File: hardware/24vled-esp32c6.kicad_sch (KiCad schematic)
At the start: 5 parts, among them J1 Conn_01x20, J2 Conn_01x20, J3 Barrel_Jack, J5 2604-1106, U1 LM2596S-5

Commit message: hardware v1
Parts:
- removed J1, J2: Conn_01x20, Connector_PinHeader_2.54mm:PinHeader_1x20_P2.54mm_Vertical, symbol Connector_Generic:Conn_01x20
- removed U1: LM2596S-5, Package_TO_SOT_SMD:TO-263-5_TabPin3, symbol Regulator_Switching:LM2596S-5
- added Q1, Q2, Q3, Q4, Q5: AO3400A, Package_TO_SOT_SMD:SOT-23, symbol Transistor_FET:AO3400A
- added R1, R3, R5, R7, R9: 100, Resistor_SMD:R_0201_0603Metric, symbol Device:R
- added R10, R2, R4, R6, R8: 10k, Resistor_SMD:R_0201_0603Metric, symbol Device:R
- added U1: R-78E5.0-1.0, Converter_DCDC:Converter_DCDC_RECOM_R-78E-0.5_THT, symbol Regulator_Switching:R-78E5.0-1.0
- added U2: ~, Library:Waveshare ESP32c6, symbol Symbols:Waveshare_ESP32c6
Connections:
- net +5V: now also U1.3 (OUT), U2.14 (Pin_14)
- net GND: now also J3.2, Q1.3 (D), Q2.3 (D), Q3.3 (D), Q4.3 (D), Q5.3 (D), R10.2, R2.2, R4.2, R6.2, R8.2, U1.2 (GND), U2.15 (Pin_15)
- net +24V: now reaches J5.1 (1_1)
- net +24V: now also J3.1, U1.1 (IN)
- net WW24: now reaches J5.11 (6_1)
- net WW24: now also Q5.2 (S)
- net R24: now reaches J5.3 (2_1)
- net R24: now also Q1.2 (S)
- net G24: now reaches J5.5 (3_1)
- net G24: now also Q2.2 (S)
- net B24: now reaches J5.7 (4_1)
- net B24: now also Q3.2 (S)
- net CW24: now reaches J5.9 (5_1)
- net CW24: now also Q4.2 (S)
- new net: Q2.1 (G), R3.2, R4.1
- new net: Q3.1 (G), R5.2, R6.1
- new net: Q5.1 (G), R10.1, R9.2
- new net: Q1.1 (G), R1.2, R2.1
- new net: Q4.1 (G), R7.2, R8.1
- new net B3.3: R5.1, U2.10 (Pin_10)
- new net CW3.3: R7.1, U2.12 (Pin_12)
- new net G3.3: R3.1, U2.8 (Pin_8)
- new net R3.3: R1.1, U2.7 (Pin_7)
- new net WW3.3: R9.1, U2.13 (Pin_13)
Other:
- moved on the sheet: J3, J5

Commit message: hardware v2
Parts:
- removed J5: 2604-1106, Wago:CONN6_2604-1106_WAG, symbol Wago:2604-1106
- added J1: 2601-1106, External:26011106, symbol External:2601-1106
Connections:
- net +24V: now also J1.1 (1.1)
- net B24: now also J1.7 (4.1)
- net CW24: now also J1.9 (5.1)
- net CW3.3: now also U2.8 (Pin_8); no longer U2.12 (Pin_12)
- net G24: now also J1.5 (3.1)
- net G3.3: now also U2.12 (Pin_12); no longer U2.8 (Pin_8)
- net R24: now also J1.3 (2.1)
- net R3.3: now also U2.13 (Pin_13); no longer U2.7 (Pin_7)
- net WW24: now also J1.11 (6.1)
- net WW3.3: now also U2.7 (Pin_7); no longer U2.13 (Pin_13)

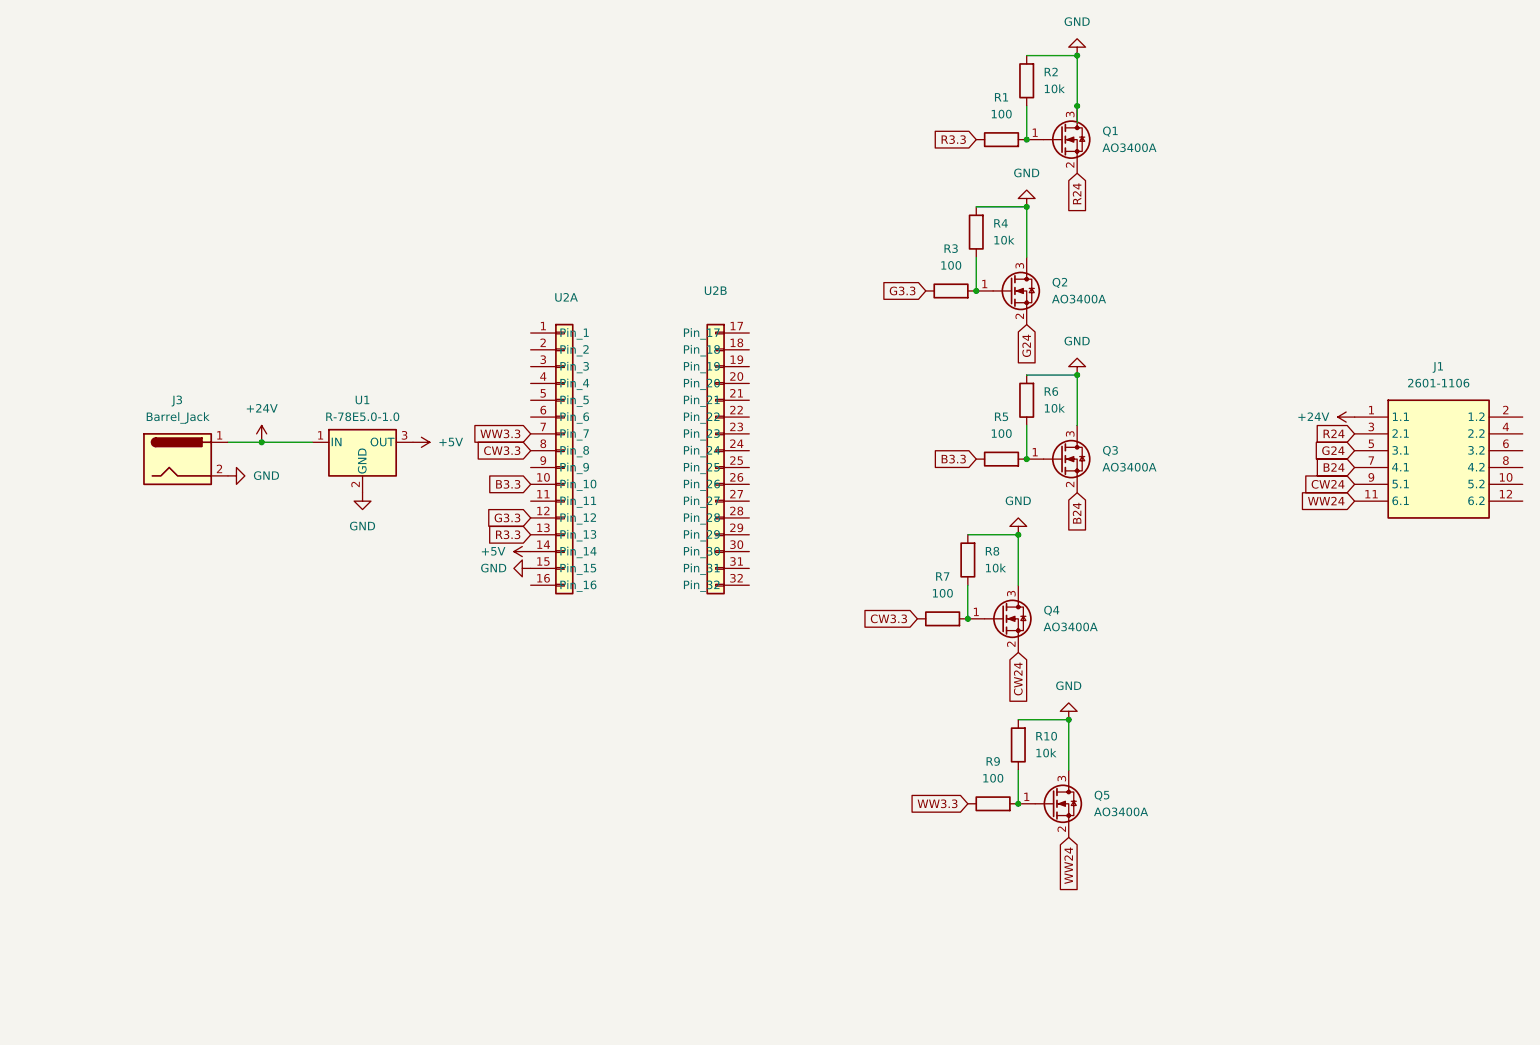
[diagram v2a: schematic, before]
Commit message: fix schematic warnings and kibot
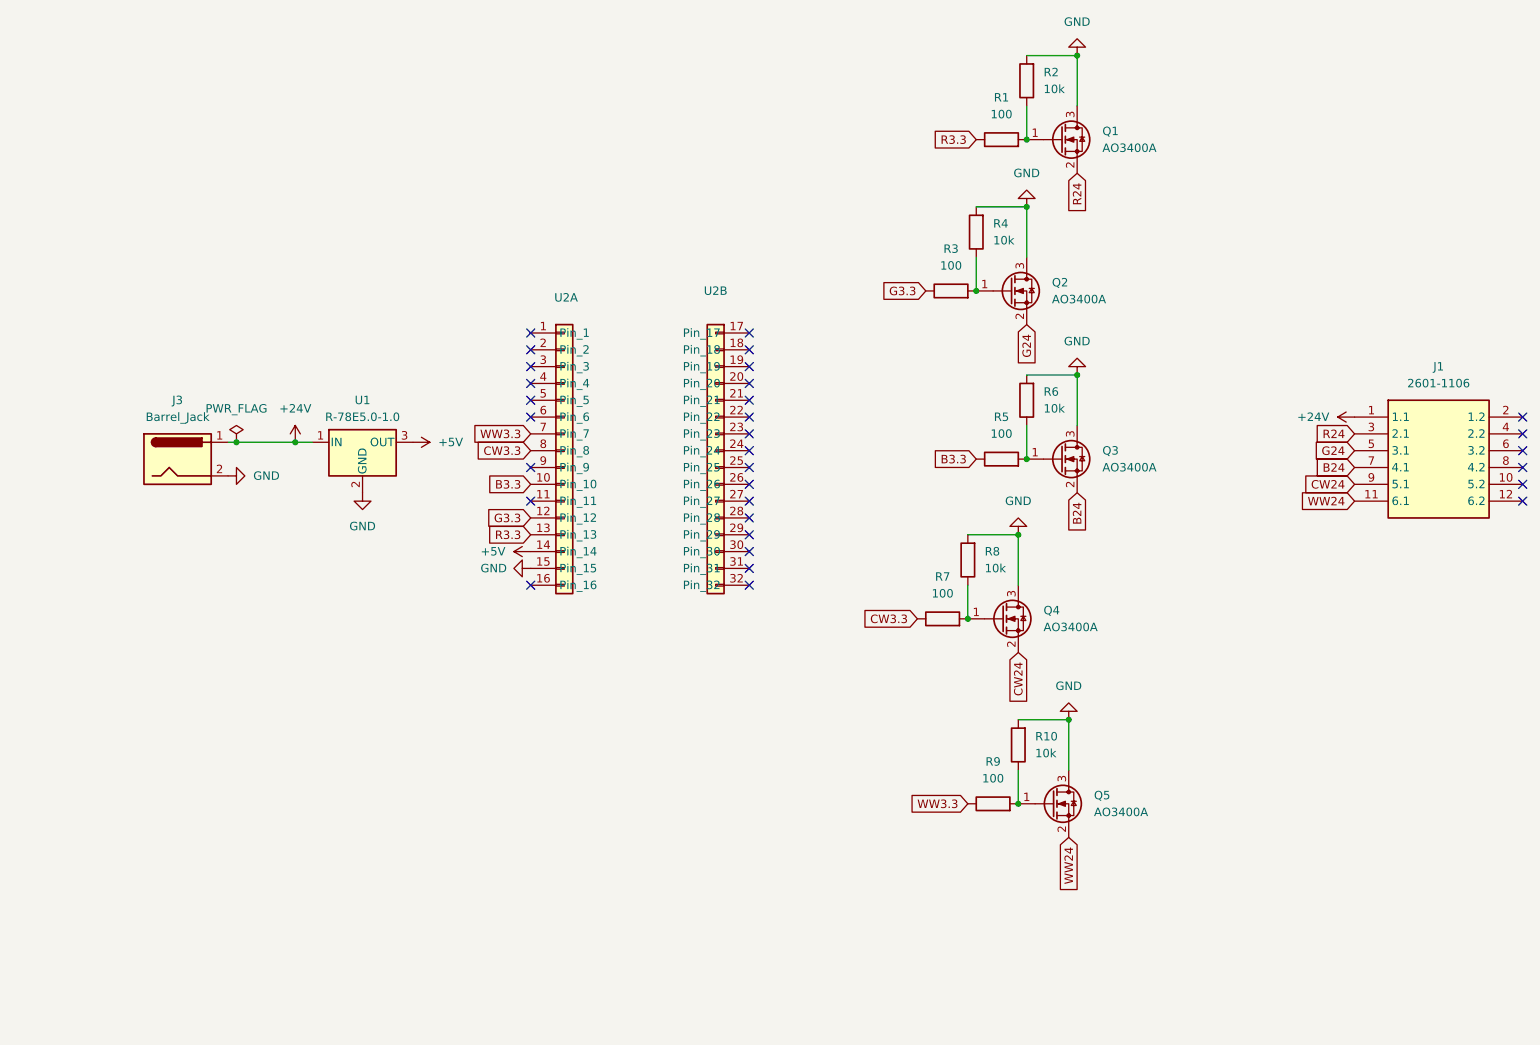
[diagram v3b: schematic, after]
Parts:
- U2: footprint Library:Waveshare ESP32c6 -> Internal:Waveshare ESP32c6; symbol Symbols:Waveshare_ESP32c6 -> Internal:Waveshare_ESP32c6
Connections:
- no-connect marks 0 -> 31
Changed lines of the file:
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@@
 	(paper "A4")
+	(junction
+		(at 57.15 87.63)
+		(diameter 0)
+		(color 0 0 0 0)
+	)
 	(junction
 		(at 175.26 142.24)
@@
 	)
 	(junction
+		(at 66.04 87.63)
+		(diameter 0)
+		(color 0 0 0 0)
+	)
+	(junction
 		(at 184.15 29.21)
 		(diameter 0)
@@
 	)
 	(junction
-		(at 184.15 36.83)
-		(diameter 0)
-		(color 0 0 0 0)
-	)
-	(junction
 		(at 168.91 64.77)
 		(diameter 0)
@@
 		(color 0 0 0 0)
 	)
-	(junction
-		(at 60.96 87.63)
-		(diameter 0)
-		(color 0 0 0 0)
+	(no_connect
+		(at 101.6 83.82)
+	)
+	(no_connect
+		(at 251.46 86.36)
+	)
+	(no_connect
+		(at 251.46 91.44)
+	)
+	(no_connect
+		(at 134.62 109.22)
+	)
+	(no_connect
+		(at 134.62 71.12)
+	)
+	(no_connect
+		(at 134.62 106.68)
+	)
+	(no_connect
+		(at 134.62 86.36)
+	)
+	(no_connect
+		(at 134.62 81.28)
+	)
+	(no_connect
+		(at 134.62 78.74)
+	)
+	(no_connect
+		(at 101.6 78.74)
+	)
+	(no_connect
+		(at 134.62 91.44)
+	)
+	(no_connect
+		(at 251.46 88.9)
+	)
+	(no_connect
+		(at 134.62 96.52)
+	)
+	(no_connect
+		(at 101.6 71.12)
+	)
+	(no_connect
+		(at 251.46 83.82)
+	)
+	(no_connect
+		(at 134.62 104.14)
+	)
+	(no_connect
+		(at 134.62 76.2)
+	)
+	(no_connect
+		(at 134.62 73.66)
+	)
+	(no_connect
+		(at 101.6 73.66)
+	)
+	(no_connect
+		(at 101.6 109.22)
+	)
+	(no_connect
+		(at 134.62 93.98)
+	)
+	(no_connect
+		(at 134.62 83.82)
+	)
+	(no_connect
+		(at 101.6 76.2)
+	)
+	(no_connect
+		(at 251.46 93.98)
+	)
+	(no_connect
+		(at 134.62 88.9)
+	)
+	(no_connect
+		(at 101.6 81.28)
+	)
+	(no_connect
+		(at 251.46 96.52)
+	)
+	(no_connect
+		(at 101.6 96.52)
+	)
+	(no_connect
+		(at 101.6 91.44)
+	)
+	(no_connect
+		(at 134.62 101.6)
+	)
+	(no_connect
+		(at 134.62 99.06)
 	)
 	(wire
@@
 	(wire
 		(pts
-			(xy 68.58 87.63) (xy 60.96 87.63)
+			(xy 184.15 29.21) (xy 184.15 36.83)
 		)
 		(stroke
@@
 	(wire
 		(pts
-			(xy 176.53 77.47) (xy 184.15 77.47)
+			(xy 68.58 87.63) (xy 66.04 87.63)
 		)
 		(stroke
@@
 	(wire
 		(pts
-			(xy 184.15 36.83) (xy 184.15 29.21)
+			(xy 176.53 77.47) (xy 184.15 77.47)
 		)
 		(stroke
@@
 	(wire
 		(pts
-			(xy 176.53 85.09) (xy 176.53 90.17)
+			(xy 57.15 87.63) (xy 55.88 87.63)
 		)
 		(stroke
@@
 	(wire
 		(pts
-			(xy 168.91 52.07) (xy 176.53 52.07)
+			(xy 176.53 85.09) (xy 176.53 90.17)
 		)
 		(stroke
@@
 	(wire
 		(pts
-			(xy 60.96 87.63) (xy 55.88 87.63)
+			(xy 168.91 52.07) (xy 176.53 52.07)
 		)
 		(stroke
@@
 	(wire
 		(pts
-			(xy 167.64 101.6) (xy 175.26 101.6)
+			(xy 57.15 87.63) (xy 66.04 87.63)
 		)
 		(stroke
@@
 	(wire
 		(pts
-			(xy 167.64 109.22) (xy 167.64 114.3)
+			(xy 167.64 101.6) (xy 175.26 101.6)
 		)
 		(stroke
@@
 	(wire
 		(pts
-			(xy 182.88 129.54) (xy 182.88 137.16)
+			(xy 167.64 109.22) (xy 167.64 114.3)
 		)
 		(stroke
@@
 	(wire
 		(pts
-			(xy 176.53 29.21) (xy 184.15 29.21)
+			(xy 182.88 129.54) (xy 182.88 137.16)
 		)
 		(stroke
@@
 	(wire
 		(pts
-			(xy 176.53 52.07) (xy 176.53 59.69)
+			(xy 176.53 29.21) (xy 184.15 29.21)
 		)
 		(stroke
@@
 	(wire
 		(pts
-			(xy 184.15 36.83) (xy 184.15 39.37)
+			(xy 176.53 52.07) (xy 176.53 59.69)
 		)
 		(stroke
@@
 	)
 	(symbol
+		(lib_id "power:PWR_FLAG")
+		(at 57.15 87.63 0)
+		(unit 1)
+		(exclude_from_sim no)
+		(in_bom yes)
+		(on_board yes)
+		(dnp no)
+		(fields_autoplaced yes)
+		(property "Reference" "#FLG01"
+			(at 57.15 85.725 0)
+			(effects
+				(font
+					(size 1.27 1.27)
+				)
+				(hide yes)
+			)
+		)
+		(property "Value" "PWR_FLAG"
+			(at 57.15 82.55 0)
+			(effects
+				(font
+					(size 1.27 1.27)
+				)
+			)
+		)
+		(property "Footprint" ""
+			(at 57.15 87.63 0)
+			(effects
+				(font
+					(size 1.27 1.27)
+				)
+				(hide yes)
+			)
+		)
+		(property "Datasheet" "~"
+			(at 57.15 87.63 0)
+			(effects
+				(font
+					(size 1.27 1.27)
+				)
+				(hide yes)
+			)
+		)
+		(property "Description" "Special symbol for telling ERC where power comes from"
+			(at 57.15 87.63 0)
+			(effects
+				(font
+					(size 1.27 1.27)
+				)
+				(hide yes)
+			)
+		)
+		(pin "1"
+		)
+		(instances
+			(project ""
+				(path "/485764ed-5b69-4a83-9e01-a6e159d31563"
+					(reference "#FLG01")
+					(unit 1)
+				)
+			)
+		)
+	)
+	(symbol
 		(lib_id "Transistor_FET:AO3400A")
 		(at 181.61 41.91 0)
@@
 	(symbol
 		(lib_id "power:+24V")
-		(at 60.96 87.63 0)
+		(at 66.04 87.63 0)
 		(unit 1)
 		(exclude_from_sim no)
@@
 		(fields_autoplaced yes)
 		(property "Reference" "#PWR04"
-			(at 60.96 91.44 0)
+			(at 66.04 91.44 0)
 			(effects
 				(font
@@
 		)
 		(property "Value" "+24V"
-			(at 60.96 82.55 0)
+			(at 66.04 82.55 0)
 			(effects
 				(font
@@
 		)
 		(property "Footprint" ""
-			(at 60.96 87.63 0)
+			(at 66.04 87.63 0)
 			(effects
 				(font
@@
 		)
 		(property "Datasheet" ""
-			(at 60.96 87.63 0)
+			(at 66.04 87.63 0)
 			(effects
 				(font
@@
 		)
 		(property "Description" "Power symbol creates a global label with name \"+24V\""
-			(at 60.96 87.63 0)
+			(at 66.04 87.63 0)
 			(effects
 				(font
@@
 	)
 	(symbol
-		(lib_id "Symbols:Waveshare_ESP32c6")
+		(lib_id "Internal:Waveshare_ESP32c6")
 		(at 120.65 90.17 0)
 		(unit 2)
@@
 			)
 		)
-		(property "Footprint" "Library:Waveshare ESP32c6"
+		(property "Footprint" "Internal:Waveshare ESP32c6"
 			(at 120.65 90.17 0)
 			(effects
@@
 	)
 	(symbol
-		(lib_id "Symbols:Waveshare_ESP32c6")
+		(lib_id "Internal:Waveshare_ESP32c6")
 		(at 114.3 90.17 0)
 		(unit 1)
@@
 			)
 		)
-		(property "Footprint" "Library:Waveshare ESP32c6"
+		(property "Footprint" "Internal:Waveshare ESP32c6"
 			(at 114.3 90.17 0)
 			(effects

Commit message: fix all pcb warnings and use larger resistors
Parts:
- R1, R10, R2, R3, R4, R5, R6, R7, R8, R9: footprint Resistor_SMD:R_0201_0603Metric -> Resistor_SMD:R_0402_1005Metric
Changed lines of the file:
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@@
 			)
 		)
-		(property "Footprint" "Resistor_SMD:R_0201_0603Metric"
+		(property "Footprint" "Resistor_SMD:R_0402_1005Metric"
 			(at 170.688 55.88 90)
 			(effects
@@
 			)
 		)
-		(property "Footprint" "Resistor_SMD:R_0201_0603Metric"
+		(property "Footprint" "Resistor_SMD:R_0402_1005Metric"
 			(at 178.308 81.28 90)
 			(effects
@@
 			)
 		)
-		(property "Footprint" "Resistor_SMD:R_0201_0603Metric"
+		(property "Footprint" "Resistor_SMD:R_0402_1005Metric"
 			(at 163.83 116.078 90)
 			(effects
@@
 			)
 		)
-		(property "Footprint" "Resistor_SMD:R_0201_0603Metric"
+		(property "Footprint" "Resistor_SMD:R_0402_1005Metric"
 			(at 171.45 144.018 90)
 			(effects
@@
 			)
 		)
-		(property "Footprint" "Resistor_SMD:R_0201_0603Metric"
+		(property "Footprint" "Resistor_SMD:R_0402_1005Metric"
 			(at 165.1 66.548 90)
 			(effects
@@
 			)
 		)
-		(property "Footprint" "Resistor_SMD:R_0201_0603Metric"
+		(property "Footprint" "Resistor_SMD:R_0402_1005Metric"
 			(at 177.038 133.35 90)
 			(effects
@@
 			)
 		)
-		(property "Footprint" "Resistor_SMD:R_0201_0603Metric"
+		(property "Footprint" "Resistor_SMD:R_0402_1005Metric"
 			(at 172.72 91.948 90)
 			(effects
@@
 			)
 		)
-		(property "Footprint" "Resistor_SMD:R_0201_0603Metric"
+		(property "Footprint" "Resistor_SMD:R_0402_1005Metric"
 			(at 178.308 33.02 90)
 			(effects
@@
 			)
 		)
-		(property "Footprint" "Resistor_SMD:R_0201_0603Metric"
+		(property "Footprint" "Resistor_SMD:R_0402_1005Metric"
 			(at 172.72 43.688 90)
 			(effects
@@
 			)
 		)
-		(property "Footprint" "Resistor_SMD:R_0201_0603Metric"
+		(property "Footprint" "Resistor_SMD:R_0402_1005Metric"
 			(at 169.418 105.41 90)
 			(effects
